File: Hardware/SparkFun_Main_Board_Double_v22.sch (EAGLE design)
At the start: 88 parts, among them J1 MICROMOD-2222-C, J10 MICRO-SD-PUSH-PUSH-EXT-PIN, J2 Vertical Qwiic Connector, J4 QWIIC_RIGHT_ANGLE, J5 CORTEX_JTAG_DEBUG_MINIMUM_PTH, J6 MICROMOD_FUNCTION_MAIN, J7 MICROMOD_FUNCTION_MAIN, Q1 3.1A/30V/105mΩ, Q2 20V/4.2A/52mΩ/1.4W, U1 STG3856QTR, U2 MCP73831, U3 ESD Diode, U4 AP7347DQ-33W5-7K-3.3V, U5 AP7361C-33

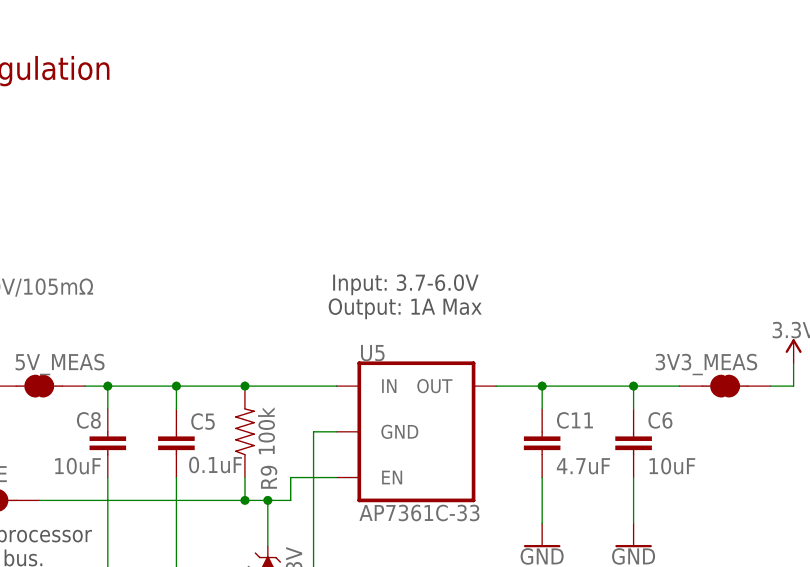
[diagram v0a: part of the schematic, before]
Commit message: Updates input voltage range on the VREG
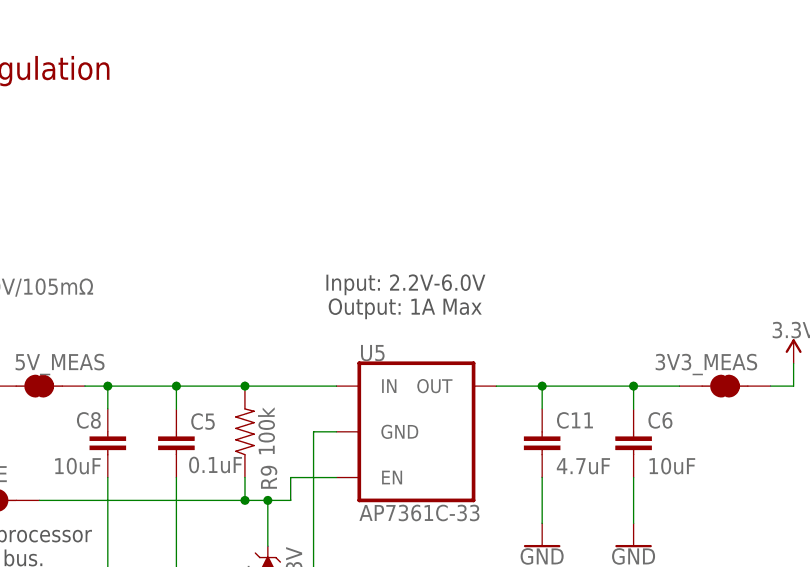
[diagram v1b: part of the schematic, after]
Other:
- note added: "Input: 2.2V-6.0V Output: 1A Max"
- note removed: "Input: 3.7-6.0V Output: 1A Max"
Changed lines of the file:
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@@
 <text x="233.68" y="263.652" size="1.778" layer="97" font="vector" align="center">Closing jumper bypasses PTC
 to allow &gt;2A current flows.</text>
-<text x="360.68" y="246.38" size="1.778" layer="97" font="vector" align="center">Input: 3.7-6.0V
+<text x="360.68" y="246.38" size="1.778" layer="97" font="vector" align="center">Input: 2.2V-6.0V
 Output: 1A Max</text>
 <text x="309.88" y="218.44" size="1.778" layer="97" font="vector" align="center">Close VE to enable processor

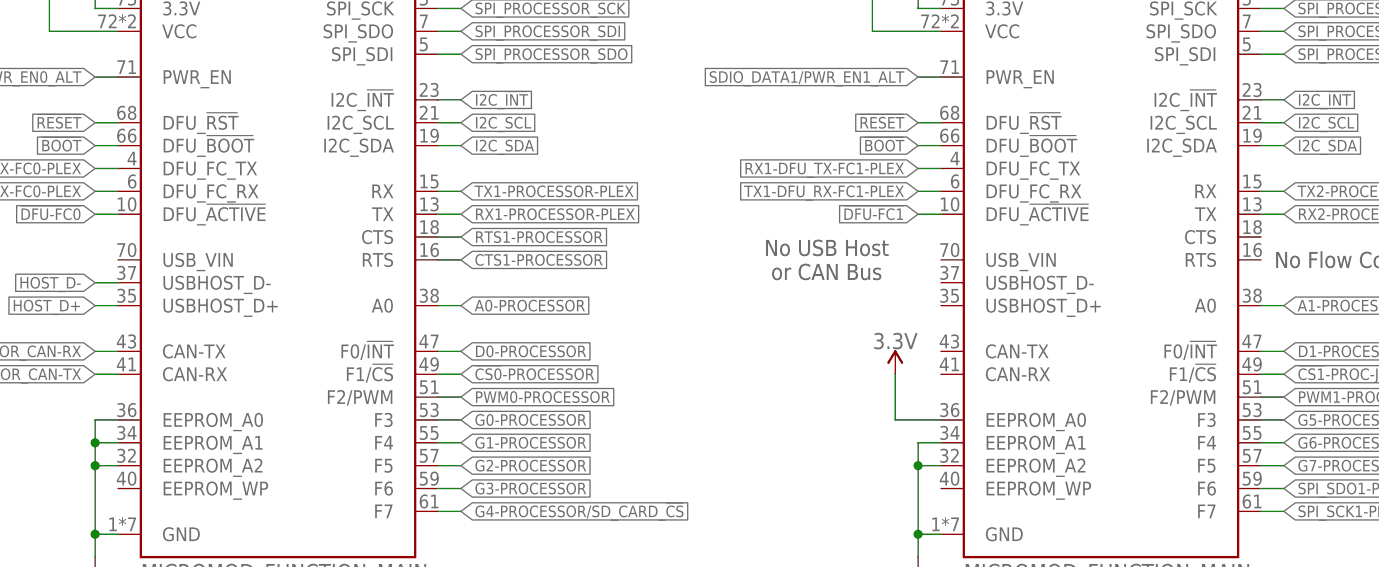
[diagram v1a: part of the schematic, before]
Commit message: Updates function board symbol
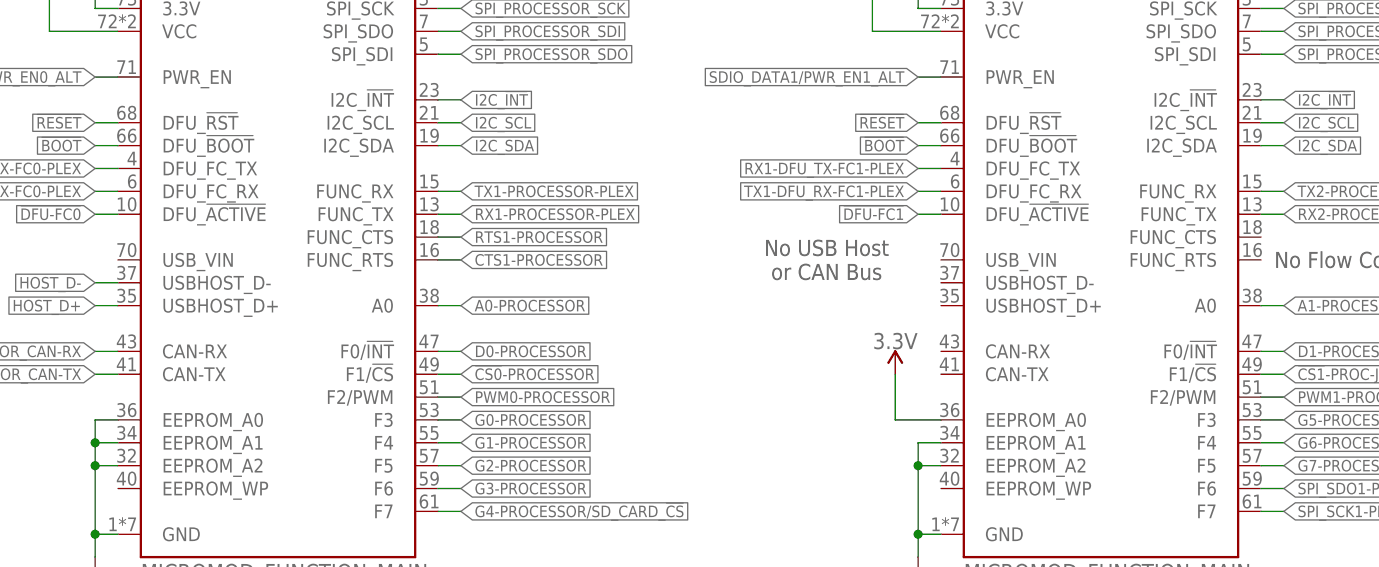
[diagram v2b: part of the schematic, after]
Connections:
- net CTS1-PROCESSOR: now also J6.FUNC_RTS; no longer J6.RTS
- net PROCESSOR_CAN-RX: now also J6.CAN-RX; no longer J6.CAN-TX
- net PROCESSOR_CAN-TX: now also J6.CAN-TX; no longer J6.CAN-RX
- net RTS1-PROCESSOR: now also J6.FUNC_CTS; no longer J6.CTS
- net RX1-PROCESSOR-PLEX: now also J6.FUNC_TX; no longer J6.TX
- net RX2-PROCESSOR: now also J7.FUNC_TX; no longer J7.TX
- net TX1-PROCESSOR-PLEX: now also J6.FUNC_RX; no longer J6.RX
- net TX2-PROCESSOR: now also J7.FUNC_RX; no longer J7.RX
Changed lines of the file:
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@@
 <wire x1="154.94" y1="86.36" x2="157.48" y2="86.36" width="0.1524" layer="91"/>
 <label x="157.48" y="86.36" size="1.27" layer="95" font="vector" xref="yes"/>
-<pinref part="J7" gate="J1" pin="RX"/>
+<pinref part="J7" gate="J1" pin="FUNC_RX"/>
 </segment>
 </net>
@@
 <wire x1="154.94" y1="83.82" x2="157.48" y2="83.82" width="0.1524" layer="91"/>
 <label x="157.48" y="83.82" size="1.27" layer="95" font="vector" xref="yes"/>
-<pinref part="J7" gate="J1" pin="TX"/>
+<pinref part="J7" gate="J1" pin="FUNC_TX"/>
 </segment>
 </net>
@@
 <wire x1="27.94" y1="66.04" x2="25.4" y2="66.04" width="0.1524" layer="91"/>
 <label x="25.4" y="66.04" size="1.27" layer="95" font="vector" rot="R180" xref="yes"/>
-<pinref part="J6" gate="J1" pin="CAN-RX"/>
+<pinref part="J6" gate="J1" pin="CAN-TX"/>
 </segment>
 </net>
@@
 <wire x1="27.94" y1="68.58" x2="25.4" y2="68.58" width="0.1524" layer="91"/>
 <label x="25.4" y="68.58" size="1.27" layer="95" font="vector" rot="R180" xref="yes"/>
-<pinref part="J6" gate="J1" pin="CAN-TX"/>
+<pinref part="J6" gate="J1" pin="CAN-RX"/>
 </segment>
 <segment>
@@
 <wire x1="63.5" y1="78.74" x2="66.04" y2="78.74" width="0.1524" layer="91"/>
 <label x="66.04" y="78.74" size="1.27" layer="95" font="vector" xref="yes"/>
-<pinref part="J6" gate="J1" pin="RTS"/>
+<pinref part="J6" gate="J1" pin="FUNC_RTS"/>
 </segment>
 </net>
@@
 <wire x1="63.5" y1="81.28" x2="66.04" y2="81.28" width="0.1524" layer="91"/>
 <label x="66.04" y="81.28" size="1.27" layer="95" font="vector" xref="yes"/>
-<pinref part="J6" gate="J1" pin="CTS"/>
+<pinref part="J6" gate="J1" pin="FUNC_CTS"/>
 </segment>
 </net>
@@
 <wire x1="63.5" y1="86.36" x2="66.04" y2="86.36" width="0.1524" layer="91"/>
 <label x="66.04" y="86.36" size="1.27" layer="95" font="vector" xref="yes"/>
-<pinref part="J6" gate="J1" pin="RX"/>
+<pinref part="J6" gate="J1" pin="FUNC_RX"/>
 </segment>
 <segment>
@@
 <wire x1="63.5" y1="83.82" x2="66.04" y2="83.82" width="0.1524" layer="91"/>
 <label x="66.04" y="83.82" size="1.27" layer="95" font="vector" xref="yes"/>
-<pinref part="J6" gate="J1" pin="TX"/>
-</segment>
-<segment>
+<pinref part="J6" gate="J1" pin="FUNC_TX"/>
+</segment>
+<segment>
